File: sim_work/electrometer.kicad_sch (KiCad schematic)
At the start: 5 parts, among them U1 LM741

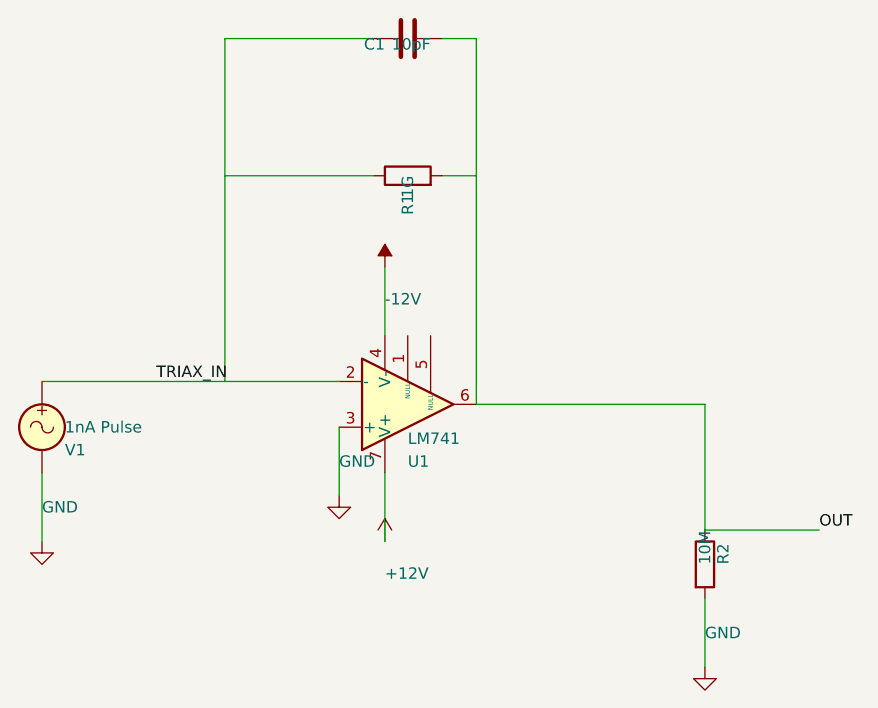
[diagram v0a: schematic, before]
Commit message: Add comparison mode, fix SimGUI subprocess popups, DAC7800 IC boxes
- SimGUI: fix Python path detection (FindPython searches Python312/313/311)
- SimGUI: suppress console popup windows (CREATE_NO_WINDOW for subprocess)
- SimGUI: add Comparison project (MDAC vs Analog oscillator side-by-side)
- SimGUI: fix async wrapping (direct await instead of Task.Run)
- Pipeline: draw DAC7800 as proper IC box with pin labels (VREF/IOUT/VCTRL)
- Pipeline: fix electrometer_362 layout (spacing, junction dots at T-junctions)
- Pipeline: fix summing amp gain annotations (BP=-0.455, not -2.2)
- Pipeline: add analog_osc command for friend's SVF oscillator simulation
- Docs: comparison_guide.md, updated README and PROJECT tracker

Co-Authored-By: Claude Opus 4.6 <noreply@anthropic.com>
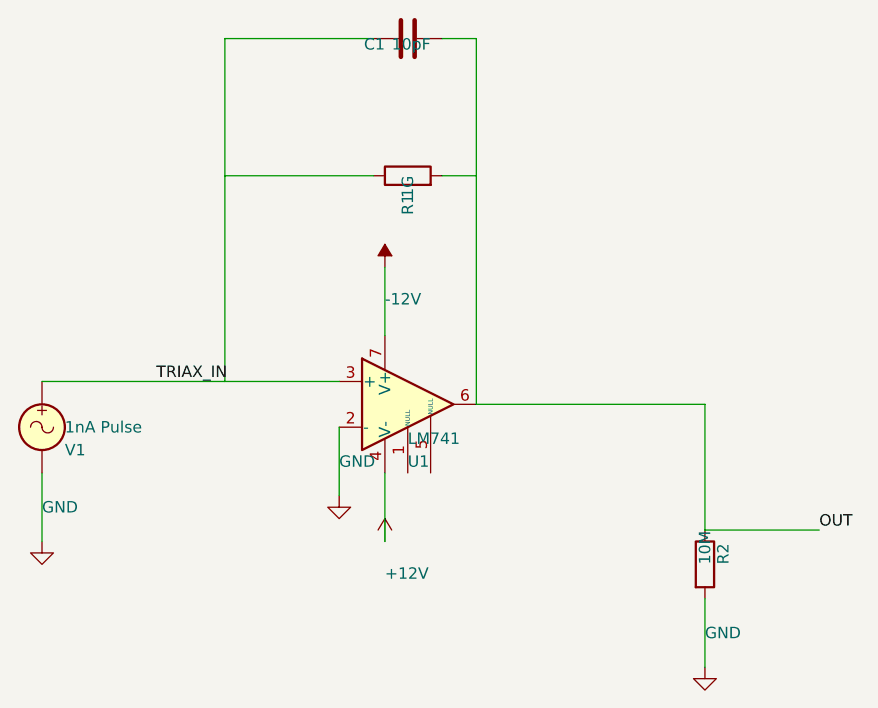
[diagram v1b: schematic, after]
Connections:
- net +12V: now also U1.4 (V-); no longer U1.7 (V+)
- net -12V: now also U1.7 (V+); no longer U1.4 (V-)
- net GND: now also U1.2 (-); no longer U1.3 (+)
- net TRIAX_IN: now also U1.3 (+); no longer U1.2 (-)
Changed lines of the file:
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@@
 		(lib_id "LM741:LM741")
 		(at 127 111.76 0)
-		(mirror x)
 		(unit 1)
 		(exclude_from_sim no)
@@
 		(instances
 			(project "Electrometer TIA"
-				(path "/43ac9c58-d0b7-48d2-9ce8-13d1d74936da"
+				(path "/b8a2ab47-be11-4a0b-b51b-4df75dac2644"
 					(reference "U1")
 					(unit 1)
@@
 		(instances
 			(project "Electrometer TIA"
-				(path "/43ac9c58-d0b7-48d2-9ce8-13d1d74936da"
+				(path "/b8a2ab47-be11-4a0b-b51b-4df75dac2644"
 					(reference "R1")
 					(unit 1)
@@
 		(instances
 			(project "Electrometer TIA"
-				(path "/43ac9c58-d0b7-48d2-9ce8-13d1d74936da"
+				(path "/b8a2ab47-be11-4a0b-b51b-4df75dac2644"
 					(reference "C1")
 					(unit 1)
@@
 		(instances
 			(project "Electrometer TIA"
-				(path "/43ac9c58-d0b7-48d2-9ce8-13d1d74936da"
+				(path "/b8a2ab47-be11-4a0b-b51b-4df75dac2644"
 					(reference "R2")
 					(unit 1)
@@
 		(instances
 			(project "Electrometer TIA"
-				(path "/43ac9c58-d0b7-48d2-9ce8-13d1d74936da"
+				(path "/b8a2ab47-be11-4a0b-b51b-4df75dac2644"
 					(reference "#PWR01")
 					(unit 1)
@@
 		(instances
 			(project "Electrometer TIA"
-				(path "/43ac9c58-d0b7-48d2-9ce8-13d1d74936da"
+				(path "/b8a2ab47-be11-4a0b-b51b-4df75dac2644"
 					(reference "#PWR02")
 					(unit 1)
@@
 		(instances
 			(project "Electrometer TIA"
-				(path "/43ac9c58-d0b7-48d2-9ce8-13d1d74936da"
+				(path "/b8a2ab47-be11-4a0b-b51b-4df75dac2644"
 					(reference "#PWR03")
 					(unit 1)
@@
 		(instances
 			(project "Electrometer TIA"
-				(path "/43ac9c58-d0b7-48d2-9ce8-13d1d74936da"
+				(path "/b8a2ab47-be11-4a0b-b51b-4df75dac2644"
 					(reference "#PWR04")
 					(unit 1)
@@
 		(instances
 			(project "Electrometer TIA"
-				(path "/43ac9c58-d0b7-48d2-9ce8-13d1d74936da"
+				(path "/b8a2ab47-be11-4a0b-b51b-4df75dac2644"
 					(reference "V1")
 					(unit 1)
@@
 		(instances
 			(project "Electrometer TIA"
-				(path "/43ac9c58-d0b7-48d2-9ce8-13d1d74936da"
+				(path "/b8a2ab47-be11-4a0b-b51b-4df75dac2644"
 					(reference "#PWR05")
 					(unit 1)
